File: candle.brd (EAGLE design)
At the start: 100 x 29 mm, 344 parts, among them U1 ATXMEGA_E5_TQFP, U2 SPW2430HR5H_B, U3 S25FL, U4 STP16CPC26TSSOP24

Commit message: Removed microphone and some connectors
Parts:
- removed C10, C7: 1u, Sebastian:0805
- removed C4: .1u, Sebastian:0805
- removed C5: (no value), Sebastian:1206_POL
- removed C8: 10n, Sebastian:0805
- removed TP16: TPB1,27, testpad:B1,27
- removed U2: SPW2430HR5H_B, Sebastian:SPW2430HR5H_B
- removed U5: (no value), Sebastian 2:TSOP5
- removed USB1: USB_MICRO_FCI_REAR_PEGS, Sebastian:USB_MICRO_FCI_REAR_PEGS
- added R38: 10k, Sebastian 2:0603
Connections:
- removed net MIC: TP16.TP, U1.24, U2.4
- removed net N$13: C8.1, U5.4
- net !FLASH_CS: now also R38.1
- net COL0: now also Q1.3; no longer Q1.2
- net GND: no longer C10.2, C4.2, C5.2, C7.2, C8.2, U2.2, U2.3, U5.2, USB1.4, USB1.5, USB1.P$3, USB1.P$4
- net PVDD: now also Q1.2; no longer C5.1, C7.1, Q1.3, U5.1, U5.3, USB1.1
- net V+: no longer C4.1, U2.1
- net VDD: now also R38.2; no longer C10.1, U5.5
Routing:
- net MIC: track 10.2 -> 0.00 mm
- net V+: track 22.7 -> 16.9 mm
- net VDD: track 116.3 -> 111.0 mm
- net GND: track 96.0 -> 91.1 mm
- net N$13: track 3.95 -> 0.00 mm
- net PVDD: track 45.9 -> 42.2 mm

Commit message: Fixed the transistor pinout error and updated eagle
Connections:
- net !C1_ renamed N$7
- net !C2_ renamed N$13
- net !C4_ renamed N$14
- net COL1: now also Q2.3; no longer Q2.2
- net COL2: now also Q3.3; no longer Q3.2
- net COL3: now also Q4.3; no longer Q4.2
- net COL4: now also Q5.3; no longer Q5.2
- net COL5: now also Q6.3; no longer Q6.2
- net COL6: now also Q7.3; no longer Q7.2
- net COL7: now also Q8.3; no longer Q8.2
- net PVDD: now also Q2.2, Q3.2, Q4.2, Q5.2, Q6.2, Q7.2, Q8.2; no longer Q2.3, Q3.3, Q4.3, Q5.3, Q6.3, Q7.3, Q8.3
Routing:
- net COL7: track 8.22 -> 6.48 mm
- net COL3: track 7.64 -> 7.06 mm
- net COL2: track 5.64 -> 5.06 mm
- net COL1: track 7.64 -> 7.06 mm
- net COL5: track 7.64 -> 7.06 mm
- net COL4: track 5.64 -> 5.06 mm
- net COL6: track 5.64 -> 5.06 mm
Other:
- outline, holes or cut-outs redrawn

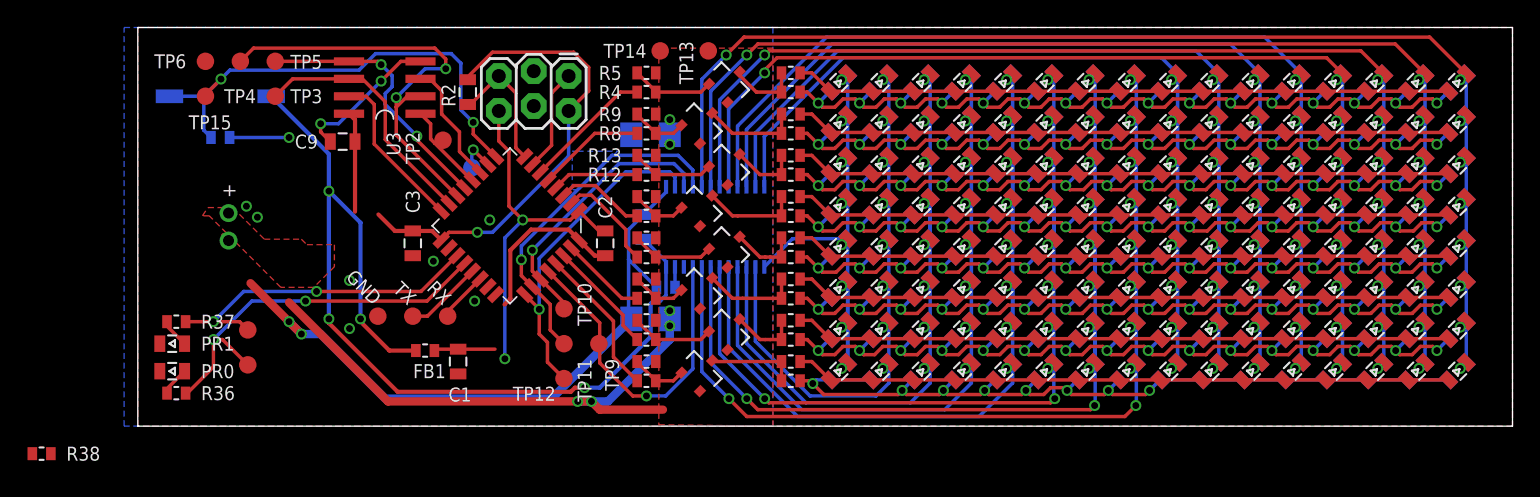
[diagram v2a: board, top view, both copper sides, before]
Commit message: Rewired the flash chip and rotated the mosfets
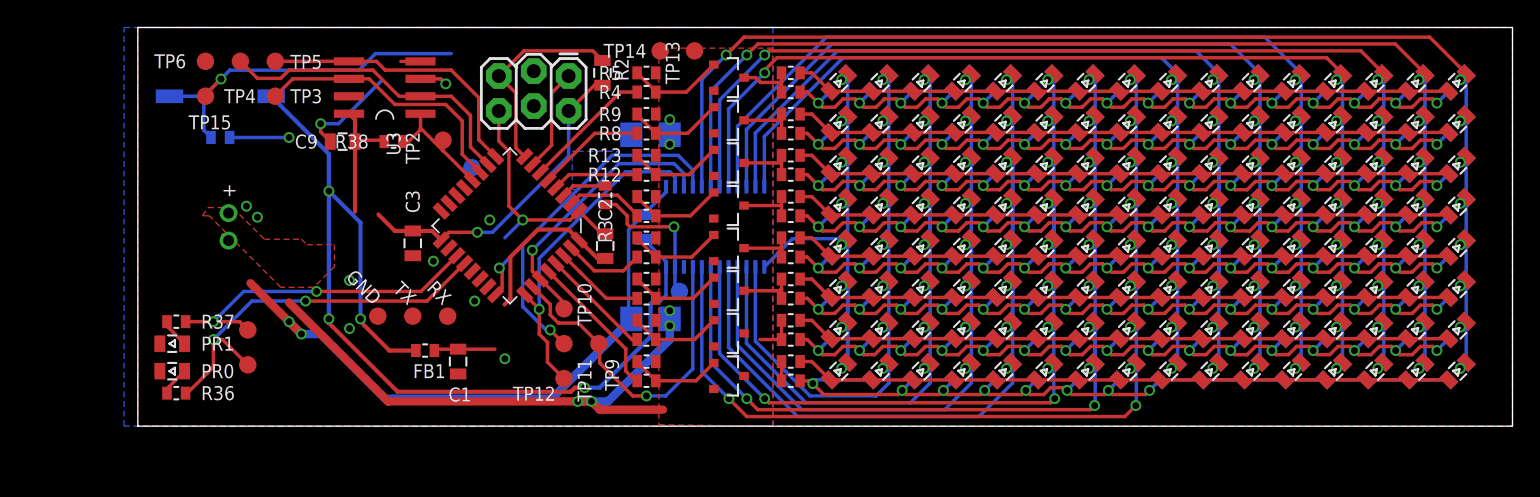
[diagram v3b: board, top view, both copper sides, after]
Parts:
- added TP16: TPB1,27, testpad:B1,27
- moved R38 34.2 mm to (18.6, 20.7), turned to 180 degrees
- moved R2 9.90 mm to (33.8, 25.7), turned to 90 degrees
- moved R3 8.02 mm to (34.0, 16.8), flipped to the top, turned to 270 degrees
- moved Q8 2.03 mm to (43.0, 3.65), turned to 270 degrees
- moved Q2 2.02 mm to (43.0, 22.2), turned to 270 degrees
- moved Q6 2.01 mm to (43.0, 9.85), turned to 270 degrees
- moved Q4 2.00 mm to (43.0, 16.1), turned to 270 degrees
- moved TP13 1.00 mm to (40.5, 27.3)
- moved Q1 0.35 mm to (43.0, 25.4), turned to 270 degrees
- moved Q7 0.25 mm to (43.0, 6.75), turned to 270 degrees
- moved C2 0.20 mm to (34.0, 13.1)
- moved Q3 0.15 mm to (43.0, 19.1), turned to 270 degrees
- moved Q5 0.05 mm to (43.0, 12.9), turned to 270 degrees
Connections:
- removed net DISP_OE!: TP9.TP, U1.28, U4.21
- removed net N$6: TP1.TP, U1.10
- new net !DISP_OE: TP9.TP, U1.26, U4.21
- new net DISP_BIAS: R3.1, U1.3
- net !C3: now also U1.2; no longer U1.3
- net !C4: now also U1.31; no longer U1.2
- net !C5: now also U1.30; no longer U1.31
- net !C6: now also U1.29; no longer U1.30
- net !C7: now also U1.28; no longer U1.29
- net !FLASH_WP: no longer U1.11
- net BTN: no longer TP15.TP, U1.9
- net DISP_LE: now also U1.24; no longer U1.26
- net FLASH_CLK: now also U1.11; no longer U1.15
- net FLASH_MISO: now also U1.10; no longer U1.14
- net FLASH_MOSI: now also U1.9; no longer U1.13
- net GND: no longer R3.1
- net N$10: now also TP16.TP
- net RXD0: no longer U1.22
- net TXD0: no longer U1.21
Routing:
- net !DISP_OE: track 0.00 -> 24.4 mm, vias 0 -> 1
- net DISP_OE!: track 24.3 -> 0.00 mm, vias 1 -> 0
- net GND: track 91.1 -> 77.5 mm, vias 14 -> 13
- net !FLASH_HOLD: track 11.9 -> 0.00 mm
- net N$10: track 1.48 -> 10.9 mm, vias 0 -> 1
- net BTN: track 35.6 -> 26.6 mm, vias 2 -> 1
- net VDD: track 111.0 -> 102.5 mm
- net FLASH_MISO: track 31.9 -> 24.9 mm, vias 2 -> 0
- net !FLASH_WP: track 8.98 -> 1.99 mm, vias 0 -> 1
- net TXD0: track 5.69 -> 0.00 mm
- net !RESET: track 9.76 -> 15.2 mm
- net COL7: track 6.48 -> 1.40 mm
- net DISP_LE: track 25.2 -> 29.9 mm, vias 1 -> 2
- net RXD0: track 3.68 -> 0.00 mm
- net DISP_BIAS: track 0.00 -> 3.32 mm
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
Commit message: Cleaned up the flash and removed unused pins
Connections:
- removed net !FLASH_HOLD: U1.16, U3.7
- removed net !FLASH_WP: U3.3
- net RXD0: now also U1.14
- net TXD0: now also U1.13
- net VDD: now also U3.3, U3.7
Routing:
- net VDD: track 102.5 -> 110.0 mm, vias 5 -> 7
- net BTN: track 26.6 -> 21.1 mm
- net GND: track 77.5 -> 79.6 mm, vias 13 -> 14
- net !FLASH_WP: track 1.99 -> 0.00 mm, vias 1 -> 0
- net FLASH_MOSI: track 20.7 -> 20.1 mm
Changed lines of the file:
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@@
 <via x="11" y="7.6" extent="1-16" drill="0.5"/>
 <wire x1="11" y1="7.6" x2="11.9" y2="6.7" width="0.6096" layer="16"/>
-<wire x1="20.56360625" y1="26.5342875" x2="19.1342875" y2="26.5342875" width="0.254" layer="1"/>
-<wire x1="17.7" y1="25.1" x2="14.6" y2="22" width="0.254" layer="16"/>
-<wire x1="14.6" y1="22" x2="13.3" y2="22" width="0.254" layer="16"/>
+<wire x1="18.5" y1="26.6" x2="13.9" y2="22" width="0.254" layer="16"/>
+<wire x1="13.9" y1="22" x2="13.3" y2="22" width="0.254" layer="16"/>
 <via x="13.3" y="22" extent="1-16" drill="0.5"/>
 <wire x1="13.3" y1="22" x2="13.3" y2="21.4" width="0.254" layer="1"/>
@@
 <wire x1="6.25" y1="13.85" x2="6.6" y2="13.5" width="0.4064" layer="1"/>
 <wire x1="6.3" y1="13.2" x2="6.6" y2="13.5" width="0.4064" layer="1"/>
+<wire x1="18.5657125" y1="26.5342875" x2="18.5" y2="26.6" width="0.254" layer="1"/>
+<via x="18.5" y="26.6" extent="1-16" drill="0.5"/>
+<wire x1="20.56360625" y1="26.5342875" x2="18.5657125" y2="26.5342875" width="0.254" layer="1"/>
+<wire x1="35.9" y1="21.2" x2="38" y2="27.3" width="0" layer="19" extent="1-16"/>
+<wire x1="38.425" y1="17.4178" x2="35.9" y2="21.2" width="0" layer="19" extent="16-16"/>
+<wire x1="34" y1="14" x2="35.7" y2="14.3" width="0" layer="19" extent="1-16"/>
+<wire x1="25.6" y1="15" x2="26.7" y2="13.7" width="0" layer="19" extent="16-16"/>
+<wire x1="15.4" y1="7.1" x2="13.3" y2="6.7" width="0" layer="19" extent="16-16"/>
+<wire x1="17.46" y1="8" x2="15.4" y2="7.1" width="0" layer="19" extent="1-1"/>
+<wire x1="15.4" y1="10.6" x2="17.46" y2="8" width="0" layer="19" extent="1-1"/>
+<wire x1="6.3" y1="13.2" x2="8.2" y2="10.4" width="0" layer="19" extent="1-1"/>
+<wire x1="7.9" y1="16" x2="6.25" y2="13.85" width="0" layer="19" extent="1-1"/>
+<wire x1="8.7" y1="15.2" x2="7.9" y2="16" width="0" layer="19" extent="1-1"/>
+<wire x1="22.640259375" y1="12.9686875" x2="25.6" y2="15" width="0" layer="19" extent="1-1"/>
+<wire x1="21.5" y1="12" x2="22.640259375" y2="12.9686875" width="0" layer="19" extent="1-1"/>
+<wire x1="20" y1="12.4" x2="21.5" y2="12" width="0" layer="19" extent="1-1"/>
+<wire x1="24.5" y1="9.1" x2="21.5" y2="12" width="0" layer="19" extent="1-1"/>
+<wire x1="26.7" y1="4.9" x2="30.1" y2="2" width="0" layer="19" extent="16-16"/>
+<wire x1="23.3" y1="3.8" x2="26.7" y2="4.9" width="0" layer="19" extent="1-1"/>
+<wire x1="6.675" y1="21" x2="7.9" y2="16" width="0" layer="19" extent="16-16"/>
+<wire x1="13.3" y1="21.4" x2="11" y2="21" width="0" layer="19" extent="1-1"/>
+<wire x1="4.92" y1="26.54" x2="6.675" y2="21" width="0" layer="19" extent="1-16"/>
+<wire x1="1.6" y1="6" x2="8.2" y2="10.4" width="0" layer="19" extent="1-1"/>
+<wire x1="1.6" y1="4" x2="1.6" y2="6" width="0" layer="19" extent="1-1"/>
 </signal>
 <signal name="VDD">
@@
 <wire x1="17.925" y1="20.7" x2="17.825" y2="20.8" width="0.254" layer="1"/>
 <wire x1="17.825" y1="20.8" x2="15.8" y2="20.8" width="0.254" layer="1"/>
+<contactref element="U3" pad="3"/>
+<contactref element="U3" pad="7"/>
+<wire x1="15.36360625" y1="23.9942875" x2="15.36360625" y2="22.7242875" width="0.254" layer="1"/>
+<wire x1="20.56360625" y1="25.2642875" x2="18.5642875" y2="25.2642875" width="0.254" layer="1"/>
+<wire x1="18.5642875" y1="25.2642875" x2="18.5" y2="25.2" width="0.254" layer="1"/>
+<via x="18.5" y="25.2" extent="1-16" drill="0.5"/>
+<wire x1="18.5" y1="25.2" x2="17.1" y2="23.8" width="0.254" layer="16"/>
+<via x="17.1" y="23.8" extent="1-16" drill="0.5"/>
+<wire x1="17.1" y1="23.8" x2="16.0242875" y2="22.7242875" width="0.254" layer="1"/>
+<wire x1="16.0242875" y1="22.7242875" x2="15.36360625" y2="22.7242875" width="0.254" layer="1"/>
 <wire x1="16.2" y1="14.8" x2="15.8" y2="15.6" width="0" layer="19" extent="1-16"/>
 <wire x1="17.5" y1="15.4" x2="16.2" y2="14.8" width="0" layer="19" extent="1-16"/>
@@
 <signal name="TXD0">
 <contactref element="TX" pad="TP"/>
+<contactref element="U1" pad="13"/>
+<wire x1="20" y1="8" x2="23.77163125" y2="17.342284375" width="0" layer="19" extent="1-1"/>
 </signal>
 <signal name="!RESET">
@@
 <wire x1="23.6" y1="19.776659375" x2="23.6" y2="22.2" width="0.254" layer="1"/>
 <wire x1="23.6" y1="22.2" x2="22.4" y2="23.4" width="0.254" layer="1"/>
-<wire x1="22.4" y1="23.4" x2="18.7" y2="23.4" width="0.254" layer="1"/>
-<wire x1="16.8357125" y1="25.2642875" x2="15.36360625" y2="25.2642875" width="0.254" layer="1"/>
-<wire x1="18.7" y1="23.4" x2="16.8357125" y2="25.2642875" width="0.254" layer="1"/>
+<wire x1="22.4" y1="23.4" x2="18.5" y2="23.4" width="0.254" layer="1"/>
+<wire x1="16.6357125" y1="25.2642875" x2="15.36360625" y2="25.2642875" width="0.254" layer="1"/>
+<wire x1="18.5" y1="23.4" x2="16.6357125" y2="25.2642875" width="0.254" layer="1"/>
 </signal>
 <signal name="FLASH_MOSI">
@@
 <wire x1="15.35789375" y1="26.54" x2="10" y2="26.54" width="0.254" layer="1"/>
 <contactref element="U1" pad="9"/>
-<wire x1="15.36360625" y1="26.5342875" x2="17.3657125" y2="26.5342875" width="0.254" layer="1"/>
-<wire x1="17.3657125" y1="26.5342875" x2="18" y2="25.9" width="0.254" layer="1"/>
-<wire x1="18" y1="25.9" x2="22.8" y2="25.9" width="0.254" layer="1"/>
-<wire x1="22.8" y1="25.9" x2="24.8" y2="23.9" width="0.254" layer="1"/>
-<wire x1="24.8" y1="23.9" x2="24.8" y2="20.839396875" width="0.254" layer="1"/>
-<wire x1="26.034371875" y1="19.605025" x2="24.8197" y2="20.819696875" width="0.254" layer="1"/>
-<wire x1="24.8197" y1="20.819696875" x2="24.8" y2="20.839396875" width="0.254" layer="1"/>
+<wire x1="15.36360625" y1="26.5342875" x2="16.9657125" y2="26.5342875" width="0.254" layer="1"/>
+<wire x1="16.9657125" y1="26.5342875" x2="17.6" y2="25.9" width="0.254" layer="1"/>
+<wire x1="17.6" y1="25.9" x2="21.8" y2="25.9" width="0.254" layer="1"/>
+<wire x1="21.8" y1="25.9" x2="24.8" y2="22.9" width="0.254" layer="1"/>
+<wire x1="24.8" y1="22.9" x2="24.8" y2="20.839396875" width="0.254" layer="1"/>
+<wire x1="26.034371875" y1="19.605025" x2="24.8" y2="20.839396875" width="0.254" layer="1"/>
 </signal>
 <signal name="!FLASH_CS">
@@
 <wire x1="24.2" y1="22.6" x2="24.2" y2="20.308028125" width="0.254" layer="1"/>
 <wire x1="7.46" y1="26.54" x2="8.7" y2="25.3" width="0.254" layer="1"/>
-<wire x1="11" y1="25.9" x2="17.1" y2="25.9" width="0.254" layer="1"/>
+<wire x1="11" y1="25.9" x2="16.8" y2="25.9" width="0.254" layer="1"/>
 <wire x1="8.7" y1="25.3" x2="10.4" y2="25.3" width="0.254" layer="1"/>
 <wire x1="10.4" y1="25.3" x2="11" y2="25.9" width="0.254" layer="1"/>
-<wire x1="17.1" y1="25.9" x2="19.0057125" y2="23.9942875" width="0.254" layer="1"/>
-<wire x1="20.56360625" y1="23.9942875" x2="19.0057125" y2="23.9942875" width="0.254" layer="1"/>
-</signal>
-<signal name="!FLASH_WP">
-<contactref element="U3" pad="3"/>
-<wire x1="20.56360625" y1="25.2642875" x2="22.0357125" y2="25.2642875" width="0.254" layer="1"/>
-<wire x1="22.0357125" y1="25.2642875" x2="22.4" y2="24.9" width="0.254" layer="1"/>
-<via x="22.4" y="24.9" extent="1-16" drill="0.5"/>
-</signal>
-<signal name="!FLASH_HOLD">
-<contactref element="U3" pad="7"/>
-<contactref element="U1" pad="16"/>
-<wire x1="22.074575" y1="15.645228125" x2="15.36360625" y2="23.9942875" width="0" layer="19" extent="1-1"/>
+<wire x1="16.8" y1="25.9" x2="18.7057125" y2="23.9942875" width="0.254" layer="1"/>
+<wire x1="20.56360625" y1="23.9942875" x2="18.7057125" y2="23.9942875" width="0.254" layer="1"/>
 </signal>
 <signal name="RXD0">
 <contactref element="RX" pad="TP"/>
+<contactref element="U1" pad="14"/>
+<wire x1="22.54" y1="8" x2="23.205946875" y2="16.7766" width="0" layer="19" extent="1-1"/>
 </signal>
 <signal name="BTN">
 <contactref element="SWT1" pad="1"/>
 <contactref element="R1" pad="2"/>
-<wire x1="22.8" y1="27.1" x2="17.3" y2="27.1" width="0.254" layer="16"/>
+<wire x1="22.8" y1="27.1" x2="17.3" y2="27.1" width="0" layer="19" extent="1-16"/>
 <wire x1="17.3" y1="27.1" x2="16.1" y2="25.9" width="0.254" layer="16"/>
 <wire x1="16.1" y1="25.9" x2="6.7" y2="25.9" width="0.254" layer="16"/>

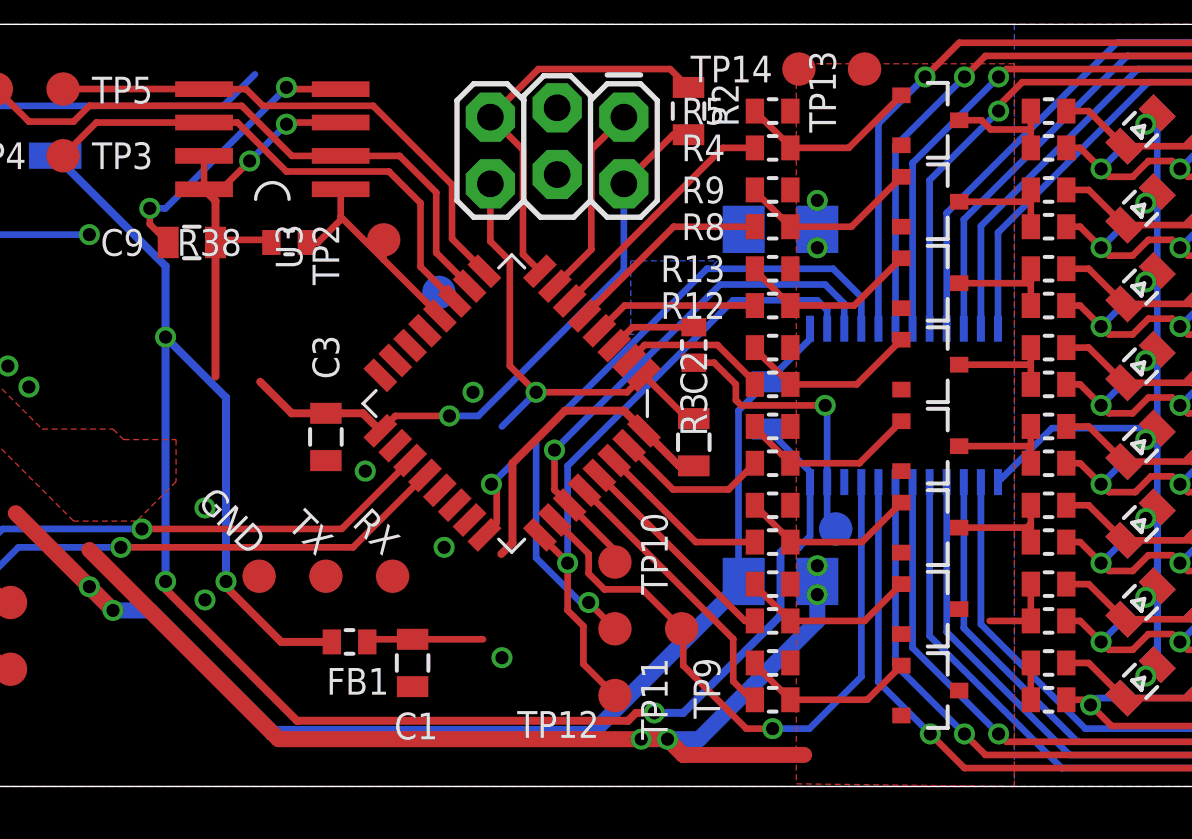
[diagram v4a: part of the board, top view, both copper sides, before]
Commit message: Added some todos and verified the flash foodprint
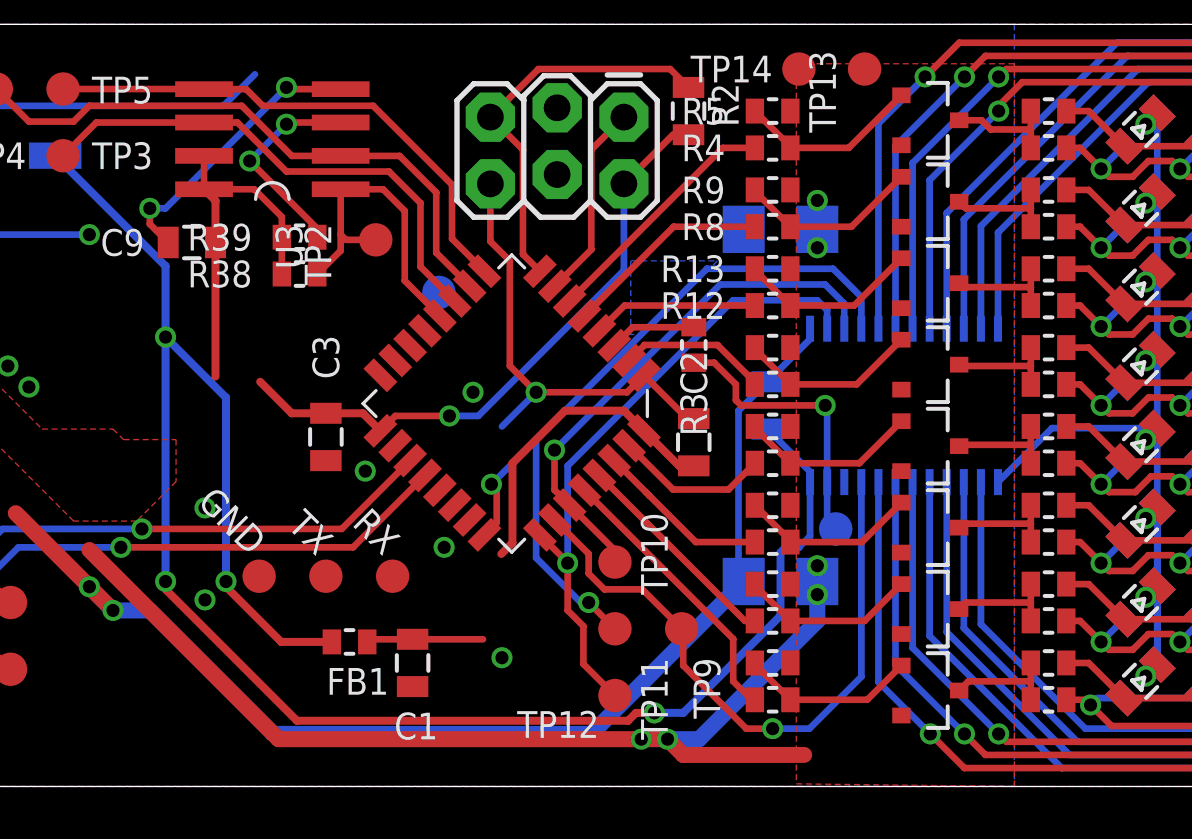
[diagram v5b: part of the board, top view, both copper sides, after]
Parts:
- added R39: 10k, Sebastian 2:0603
- moved R38 1.26 mm to (19.0, 19.5)
- moved TP2 0.30 mm to (21.9, 20.8)
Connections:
- new net N$15: U1.15
- new net N$16: U1.16
- new net N$6: R39.1, U3.3
- net VDD: now also R39.2; no longer U3.3
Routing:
- net N$6: track 0.00 -> 8.04 mm, vias 0 -> 2
- net !FLASH_CS: track 9.19 -> 12.3 mm
- net COL7: track 1.40 -> 4.27 mm
- net VDD: track 110.0 -> 107.1 mm, vias 7 -> 5
- net COL6: track 2.97 -> 4.23 mm
